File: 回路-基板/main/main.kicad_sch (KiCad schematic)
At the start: 49 parts, among them J1 Conn_01x07_Pin, J2 Conn_01x08_Pin, J3 Conn_01x08_Pin, J4 Conn_01x08_Pin, J5 Conn_01x08_Pin, SW1 SW_Push, SW2 SW_Push, SW3 SW_Push, SW4 SW_Push, SW5 SW_Push, SW6 SW_Push, SW7 SW_Push, U1 TWE-L-WX, U2 LM1117MP-3.3

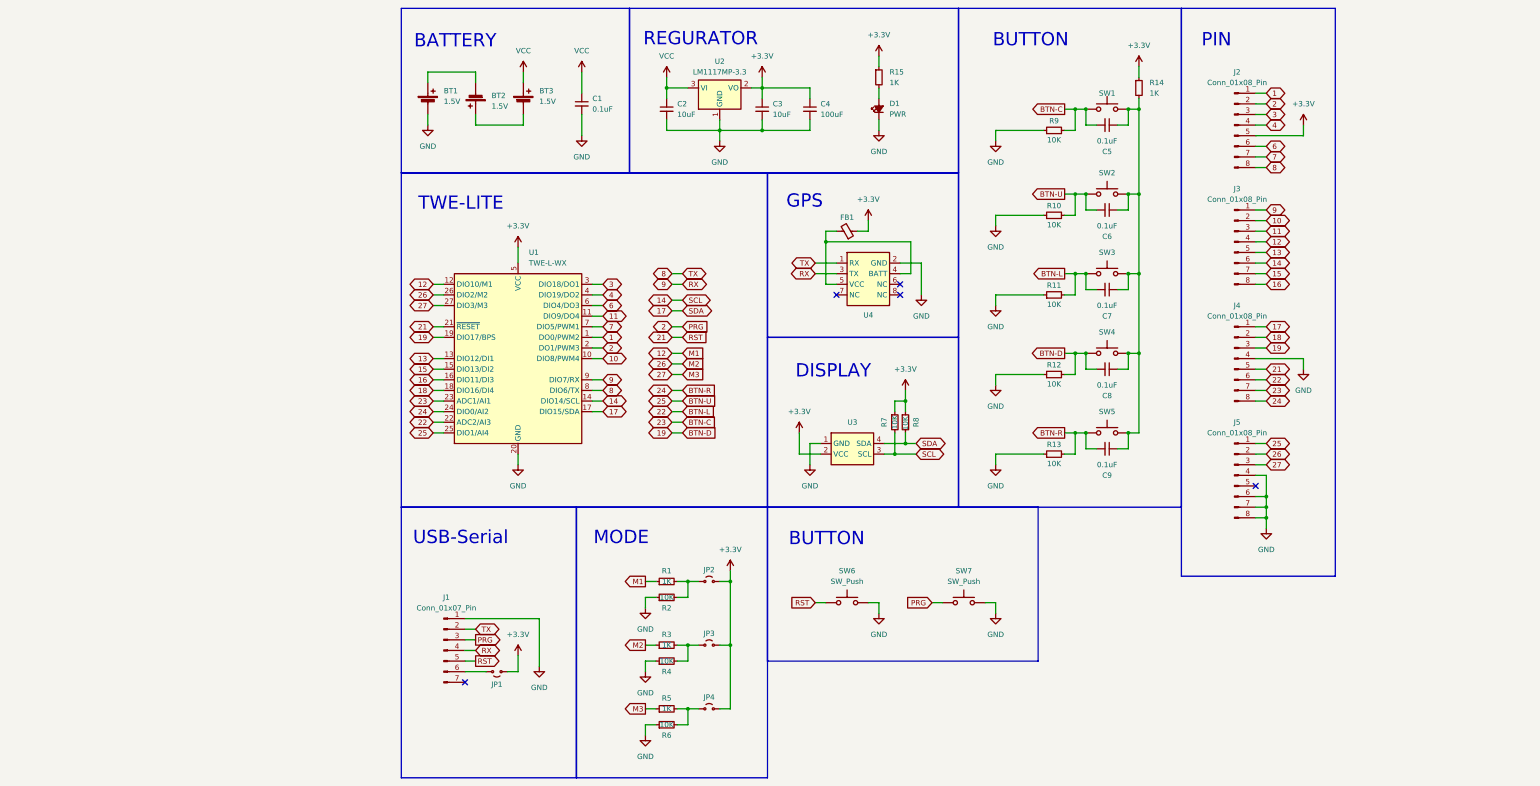
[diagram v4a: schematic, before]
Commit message: 回路図とPCBを修正した
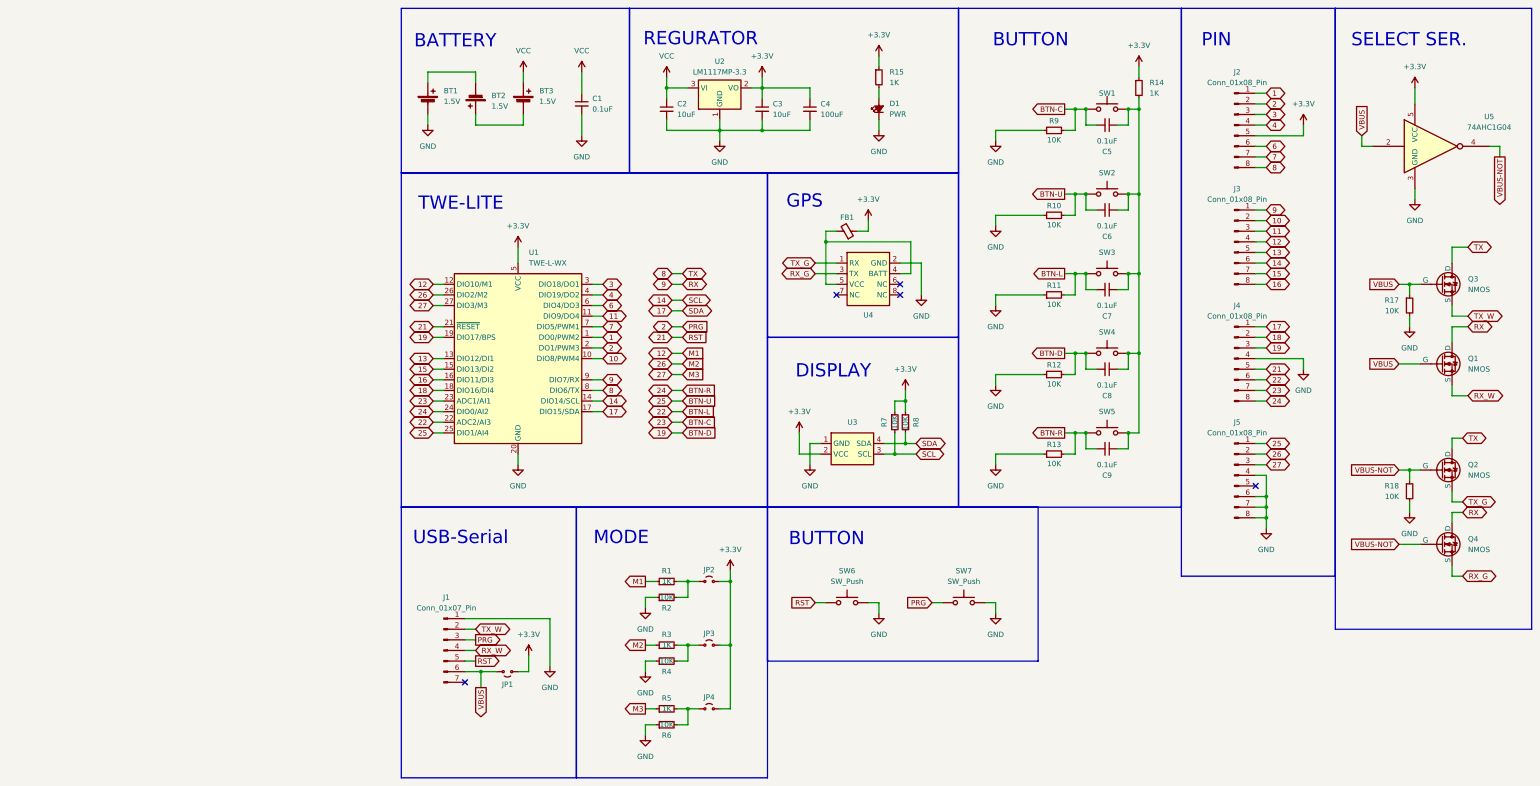
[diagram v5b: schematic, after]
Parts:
- added Q1, Q2, Q3, Q4: NMOS, Package_TO_SOT_SMD:SOT-23, symbol @2023_KickerAdjust:NMOS
- added R17, R18: 10K, Resistor_SMD:R_0805_2012Metric, symbol Device:R_Small
- added U5: 74AHC1G04, Package_TO_SOT_SMD:SOT-23-5, symbol 74xGxx:74AHC1G04
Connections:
- net +3.3V: now also U5.5 (VCC)
- net 8: now also Q2.2 (D), Q3.2 (D); no longer J1.2 (Pin_2), U4.1 (RX)
- net 9: now also Q1.2 (D), Q4.2 (D); no longer J1.4 (Pin_4), U4.3 (TX)
- net GND: now also R17.2, R18.2, U5.3 (GND)
- net VBUS: now reaches J1.6 (Pin_6), JP1.2 (B)
- net VBUS: now also Q1.1 (G), Q3.1 (G), R17.1, U5.2
- new net RX_G: Q4.3 (S), U4.3 (TX)
- new net RX_W: J1.4 (Pin_4), Q1.3 (S)
- new net TX_G: Q2.3 (S), U4.1 (RX)
- new net TX_W: J1.2 (Pin_2), Q3.3 (S)
- new net VBUS-NOT: Q2.1 (G), Q4.1 (G), R18.1, U5.4
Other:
- note added: "SELECT SER."
- moved on the sheet: JP1

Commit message: 回路図とPCBを更新
GPSの電源のオンオフ式に切り替え
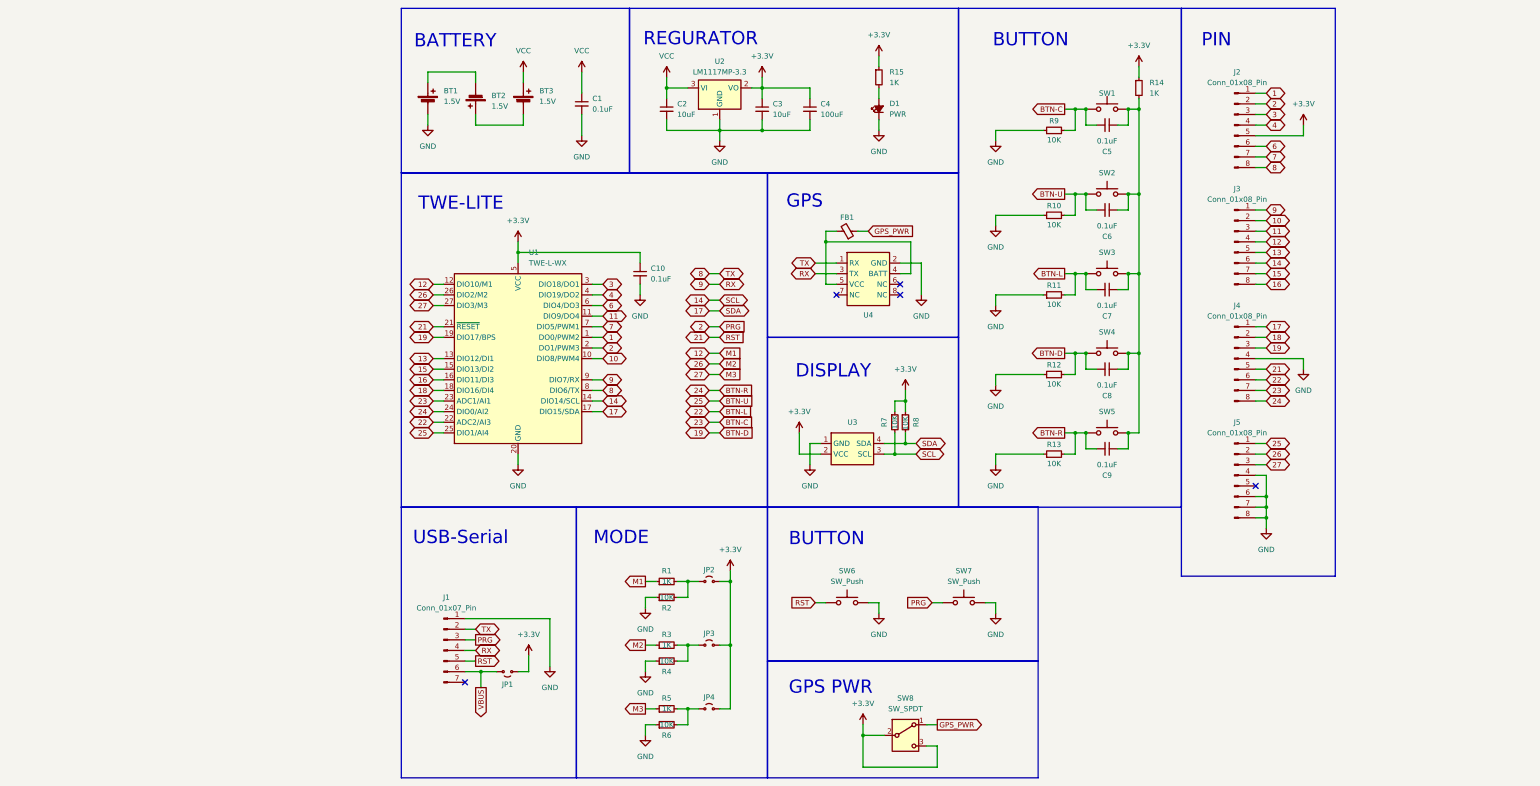
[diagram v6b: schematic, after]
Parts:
- removed Q1, Q2, Q3, Q4: NMOS, Package_TO_SOT_SMD:SOT-23, symbol @2023_KickerAdjust:NMOS
- removed R17, R18: 10K, Resistor_SMD:R_0805_2012Metric, symbol Device:R_Small
- removed U5: 74AHC1G04, Package_TO_SOT_SMD:SOT-23-5, symbol 74xGxx:74AHC1G04
- added C10: 0.1uF, Capacitor_SMD:C_0805_2012Metric, symbol Device:C_Small
- added SW8: SW_SPDT, @2024-Power:SS12D01G4, symbol Switch:SW_SPDT
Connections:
- net RX_G is gone; now on net 9: U4.3 (TX)
- net RX_W is gone; now on net 9: J1.4 (Pin_4)
- net TX_G is gone; now on net 8: U4.1 (RX)
- net TX_W is gone; now on net 8: J1.2 (Pin_2)
- net +3.3V: now also C10.1, SW8.2 (B), SW8.3 (C); no longer FB1.1
- net GND: now also C10.2
- new net GPS_PWR: FB1.1, SW8.1 (A)
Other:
- note added: "GPS PWR"
- note removed: "SELECT SER."

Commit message: ピンのテストプログラムと基板の更新版PCB
PCBのDRよろしくー
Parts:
- added D2: LED, LED_SMD:LED_0805_2012Metric, symbol Device:LED_Small_Filled
- added R16: 330, Resistor_SMD:R_0805_2012Metric, symbol Device:R_Small
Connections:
- net 15: now also R16.1
- net 16: now also C7.2, R11.2, SW3.1
- net 18: now also C5.2, R9.2, SW1.1
- net 22: no longer C7.2, R11.2, SW3.1
- net 23: no longer C5.2, R9.2, SW1.1
- net GND: now also D2.1 (K)
- new net: D2.2 (A), R16.2
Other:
- note added: "LED"

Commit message: 回路 v3 完成したよ
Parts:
- added D3: LED, LED_SMD:LED_0805_2012Metric, symbol Device:LED_Small_Filled
- added R17: 330, Resistor_SMD:R_0805_2012Metric, symbol Device:R_Small
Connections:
- net 13: now also R16.1
- net 15: now also R17.1; no longer R16.1
- net GND: now also D3.1 (K)
- new net: D3.2 (A), R17.2
